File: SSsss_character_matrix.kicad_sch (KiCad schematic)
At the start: 17 parts, among them U15 SN74LVC244A, U16 10016AS, U17 10016AS, U18 SN74LVC244A, U19 10016AS, U20 10016AS, U21 10016AS

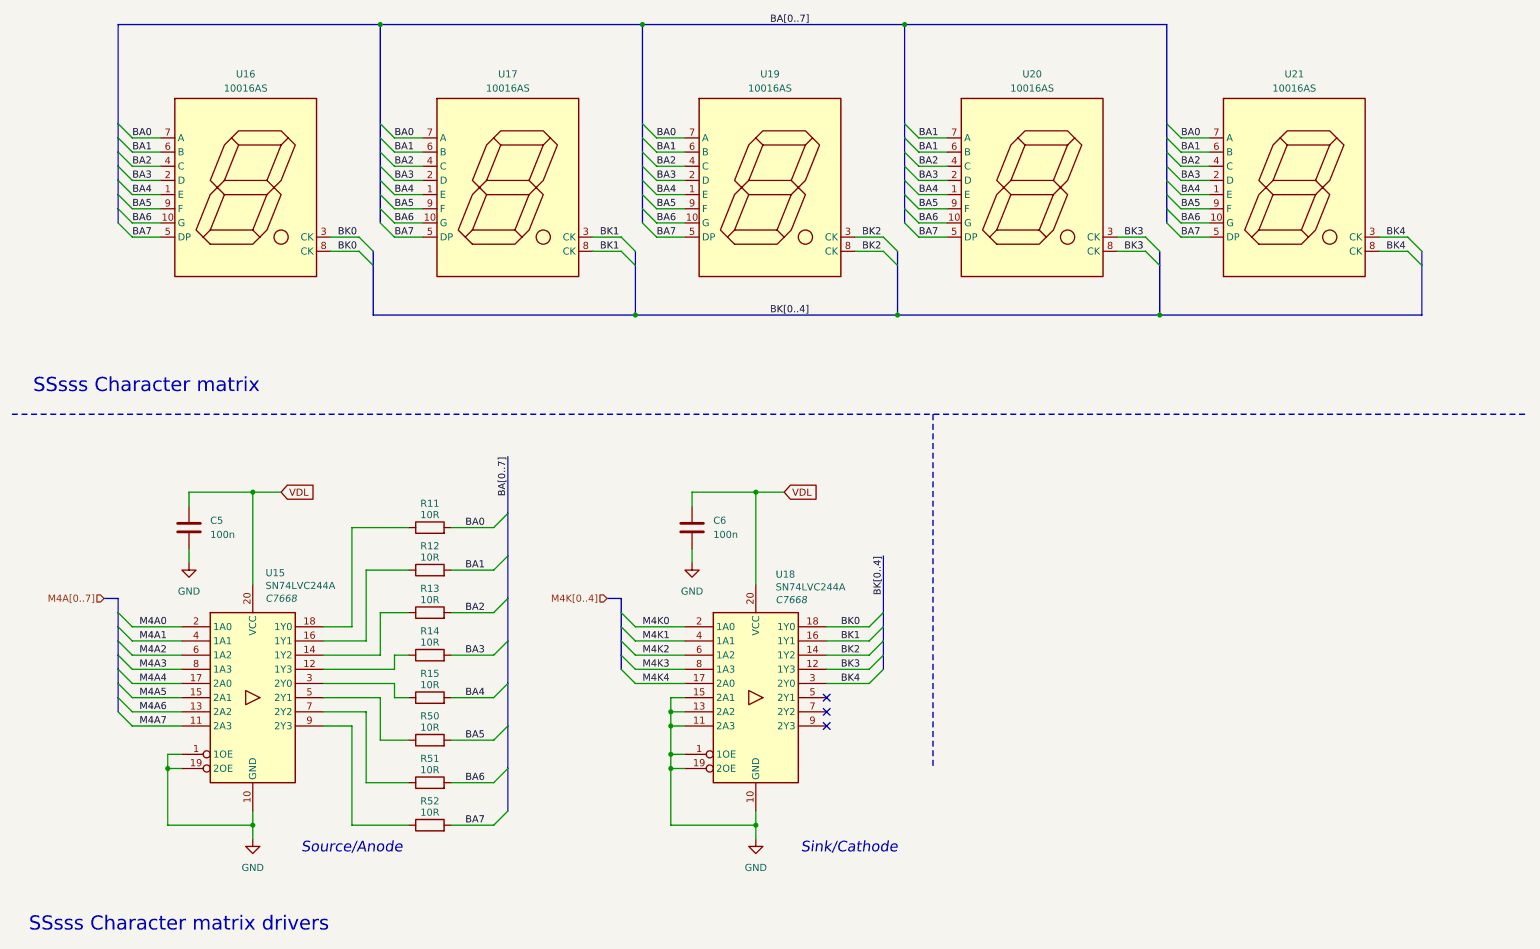
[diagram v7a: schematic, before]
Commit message: PCB routing
- JLCPCB constraints added
- removal of multiple test points
- change of footprints
- change of THT LEDs
- rough position of all the major components
- PCB routing started
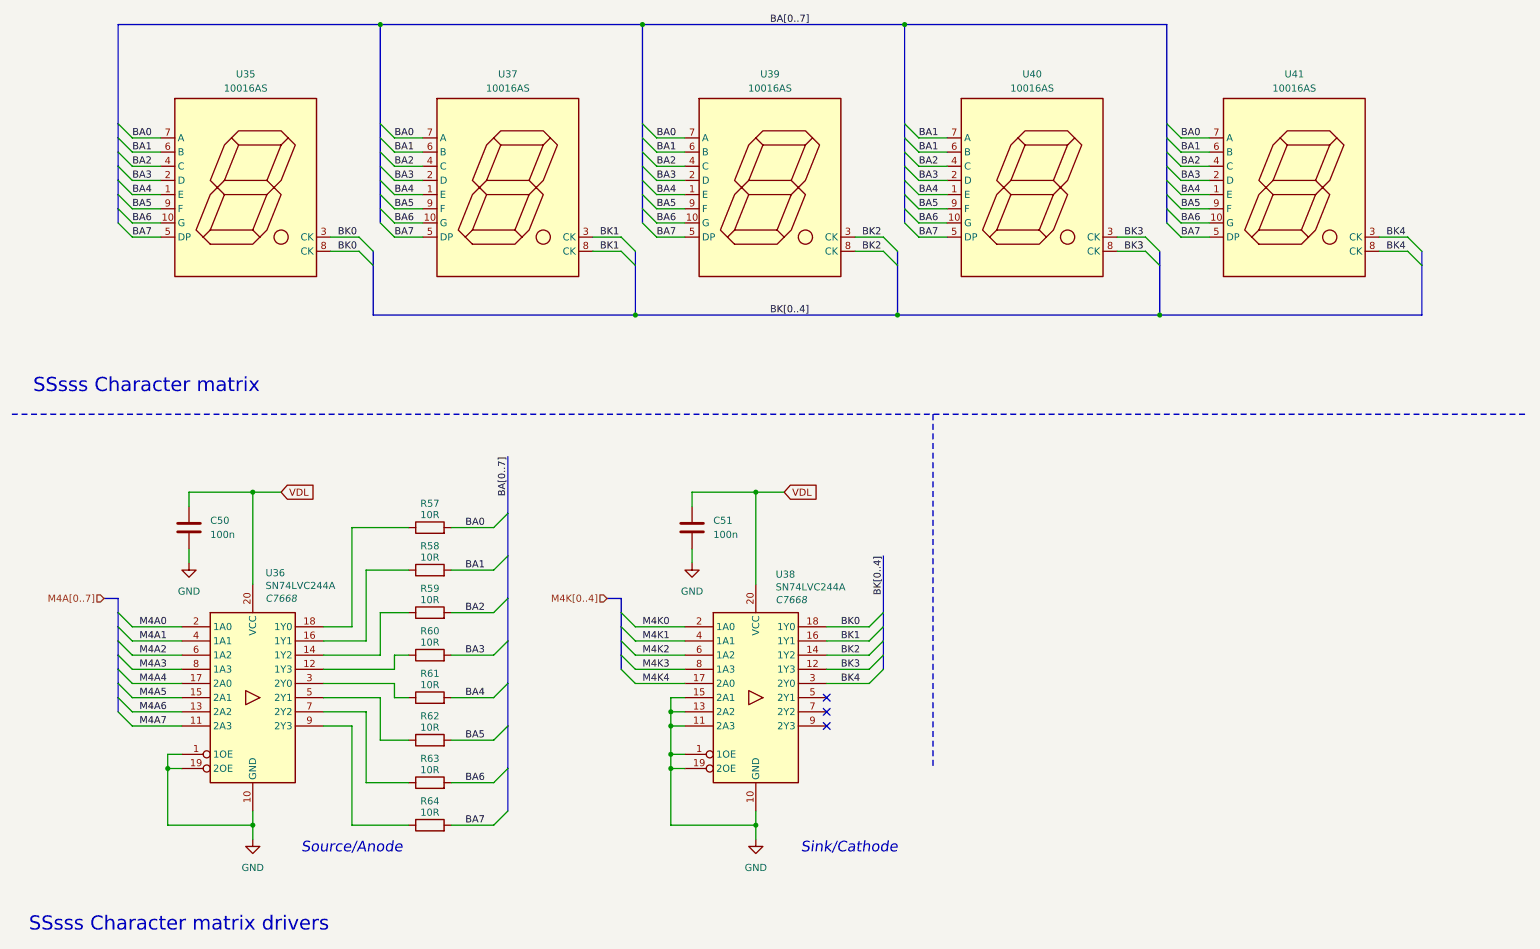
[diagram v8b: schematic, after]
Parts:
- U35: renamed from U16; footprint precision_clock:10016AS -> precision_clock:Xlitx 10016AS
- U37: renamed from U17; footprint precision_clock:10016AS -> precision_clock:Xlitx 10016AS
- U39: renamed from U19; footprint precision_clock:10016AS -> precision_clock:Xlitx 10016AS
- U40: renamed from U20; footprint precision_clock:10016AS -> precision_clock:Xlitx 10016AS
- U41: renamed from U21; footprint precision_clock:10016AS -> precision_clock:Xlitx 10016AS
- renumbered C5 to C50, C6 to C51, R11 to R57, R12 to R58, R13 to R59, R14 to R60, R15 to R61, R50 to R62, R51 to R63, R52 to R64, U15 to U36, U18 to U38
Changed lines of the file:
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@@
 		(on_board yes)
 		(dnp no)
-		(property "Reference" "R12"
+		(property "Reference" "R58"
 			(at 87.63 125.222 90)
 			(effects
@@
 			(project "Precision Clock"
 				(path "/c9a8ff63-a0d1-4125-9dd1-40fb53daf536/61b252ee-6ab4-4417-a4ad-7fc052d7ca20"
-					(reference "R12")
+					(reference "R58")
 					(unit 1)
 				)
@@
 		(dnp no)
 		(fields_autoplaced yes)
-		(property "Reference" "#PWR012"
+		(property "Reference" "#PWR0115"
 			(at 146.05 184.15 0)
 			(effects
@@
 			(project "Precision Clock"
 				(path "/c9a8ff63-a0d1-4125-9dd1-40fb53daf536/61b252ee-6ab4-4417-a4ad-7fc052d7ca20"
-					(reference "#PWR012")
+					(reference "#PWR0115")
 					(unit 1)
 				)
@@
 		(on_board yes)
 		(dnp no)
-		(property "Reference" "R51"
+		(property "Reference" "R63"
 			(at 87.63 163.322 90)
 			(effects
@@
 			(project "Precision Clock"
 				(path "/c9a8ff63-a0d1-4125-9dd1-40fb53daf536/61b252ee-6ab4-4417-a4ad-7fc052d7ca20"
-					(reference "R51")
+					(reference "R63")
 					(unit 1)
 				)
@@
 		(dnp no)
 		(fields_autoplaced yes)
-		(property "Reference" "U19"
+		(property "Reference" "U39"
 			(at 148.59 40.64 0)
 			(effects
@@
 			)
 		)
-		(property "Footprint" "precision_clock:10016AS"
+		(property "Footprint" "precision_clock:Xlitx 10016AS"
 			(at 148.59 60.96 0)
 			(effects
@@
 			(project "Precision Clock"
 				(path "/c9a8ff63-a0d1-4125-9dd1-40fb53daf536/61b252ee-6ab4-4417-a4ad-7fc052d7ca20"
-					(reference "U19")
+					(reference "U39")
 					(unit 1)
 				)
@@
 		(dnp no)
 		(fields_autoplaced yes)
-		(property "Reference" "C6"
+		(property "Reference" "C51"
 			(at 138.43 120.6499 0)
 			(effects
@@
 			(project "Precision Clock"
 				(path "/c9a8ff63-a0d1-4125-9dd1-40fb53daf536/61b252ee-6ab4-4417-a4ad-7fc052d7ca20"
-					(reference "C6")
+					(reference "C51")
 					(unit 1)
 				)
@@
 		(dnp no)
 		(fields_autoplaced yes)
-		(property "Reference" "#PWR09"
+		(property "Reference" "#PWR0112"
 			(at 44.45 134.62 0)
 			(effects
@@
 			(project "Precision Clock"
 				(path "/c9a8ff63-a0d1-4125-9dd1-40fb53daf536/61b252ee-6ab4-4417-a4ad-7fc052d7ca20"
-					(reference "#PWR09")
+					(reference "#PWR0112")
 					(unit 1)
 				)
@@
 		(dnp no)
 		(fields_autoplaced yes)
-		(property "Reference" "U21"
+		(property "Reference" "U41"
 			(at 242.57 40.64 0)
 			(effects
@@
 			)
 		)
-		(property "Footprint" "precision_clock:10016AS"
+		(property "Footprint" "precision_clock:Xlitx 10016AS"
 			(at 242.57 60.96 0)
 			(effects
@@
 			(project "Precision Clock"
 				(path "/c9a8ff63-a0d1-4125-9dd1-40fb53daf536/61b252ee-6ab4-4417-a4ad-7fc052d7ca20"
-					(reference "U21")
+					(reference "U41")
 					(unit 1)
 				)
@@
 		(on_board yes)
 		(dnp no)
-		(property "Reference" "R52"
+		(property "Reference" "R64"
 			(at 87.63 170.942 90)
 			(effects
@@
 			(project "Precision Clock"
 				(path "/c9a8ff63-a0d1-4125-9dd1-40fb53daf536/61b252ee-6ab4-4417-a4ad-7fc052d7ca20"
-					(reference "R52")
+					(reference "R64")
 					(unit 1)
 				)
@@
 		(on_board yes)
 		(dnp no)
-		(property "Reference" "U15"
+		(property "Reference" "U36"
 			(at 58.166 130.048 0)
 			(effects
@@
 			(project "Precision Clock"
 				(path "/c9a8ff63-a0d1-4125-9dd1-40fb53daf536/61b252ee-6ab4-4417-a4ad-7fc052d7ca20"
-					(reference "U15")
+					(reference "U36")
 					(unit 1)
 				)
@@
 		(on_board yes)
 		(dnp no)
-		(property "Reference" "R50"
+		(property "Reference" "R62"
 			(at 87.63 155.702 90)
 			(effects
@@
 			(project "Precision Clock"
 				(path "/c9a8ff63-a0d1-4125-9dd1-40fb53daf536/61b252ee-6ab4-4417-a4ad-7fc052d7ca20"
-					(reference "R50")
+					(reference "R62")
 					(unit 1)
 				)
@@
 		(dnp no)
 		(fields_autoplaced yes)
-		(property "Reference" "#PWR010"
+		(property "Reference" "#PWR0113"
 			(at 55.88 184.15 0)
 			(effects
@@
 			(project "Precision Clock"
 				(path "/c9a8ff63-a0d1-4125-9dd1-40fb53daf536/61b252ee-6ab4-4417-a4ad-7fc052d7ca20"
-					(reference "#PWR010")
+					(reference "#PWR0113")
 					(unit 1)
 				)
@@
 		(dnp no)
 		(fields_autoplaced yes)
-		(property "Reference" "U16"
+		(property "Reference" "U35"
 			(at 54.61 40.64 0)
 			(effects
@@
 			)
 		)
-		(property "Footprint" "precision_clock:10016AS"
+		(property "Footprint" "precision_clock:Xlitx 10016AS"
 			(at 54.61 60.96 0)
 			(effects
@@
 			(project "Precision Clock"
 				(path "/c9a8ff63-a0d1-4125-9dd1-40fb53daf536/61b252ee-6ab4-4417-a4ad-7fc052d7ca20"
-					(reference "U16")
+					(reference "U35")
 					(unit 1)
 				)
@@
 		(dnp no)
 		(fields_autoplaced yes)
-		(property "Reference" "#PWR011"
+		(property "Reference" "#PWR0114"
 			(at 134.62 134.62 0)
 			(effects
@@
 			(project "Precision Clock"
 				(path "/c9a8ff63-a0d1-4125-9dd1-40fb53daf536/61b252ee-6ab4-4417-a4ad-7fc052d7ca20"
-					(reference "#PWR011")
+					(reference "#PWR0114")
 					(unit 1)
 				)
@@
 		(dnp no)
 		(fields_autoplaced yes)
-		(property "Reference" "U20"
+		(property "Reference" "U40"
 			(at 195.58 40.64 0)
 			(effects
@@
 			)
 		)
-		(property "Footprint" "precision_clock:10016AS"
+		(property "Footprint" "precision_clock:Xlitx 10016AS"
 			(at 195.58 60.96 0)
 			(effects
@@
 			(project "Precision Clock"
 				(path "/c9a8ff63-a0d1-4125-9dd1-40fb53daf536/61b252ee-6ab4-4417-a4ad-7fc052d7ca20"
-					(reference "U20")
+					(reference "U40")
 					(unit 1)
 				)
@@
 		(dnp no)
 		(fields_autoplaced yes)
-		(property "Reference" "C5"
+		(property "Reference" "C50"
 			(at 48.26 120.6499 0)
 			(effects
@@
 			(project "Precision Clock"
 				(path "/c9a8ff63-a0d1-4125-9dd1-40fb53daf536/61b252ee-6ab4-4417-a4ad-7fc052d7ca20"
-					(reference "C5")
+					(reference "C50")
 					(unit 1)
 				)
@@
 		(on_board yes)
 		(dnp no)
-		(property "Reference" "R15"
+		(property "Reference" "R61"
 			(at 87.63 148.082 90)
 			(effects
@@
 			(project "Precision Clock"
 				(path "/c9a8ff63-a0d1-4125-9dd1-40fb53daf536/61b252ee-6ab4-4417-a4ad-7fc052d7ca20"
-					(reference "R15")
+					(reference "R61")
 					(unit 1)
 				)
@@
 		(on_board yes)
 		(dnp no)
-		(property "Reference" "R11"
+		(property "Reference" "R57"
 			(at 87.63 117.602 90)
 			(effects
@@
 			(project "Precision Clock"
 				(path "/c9a8ff63-a0d1-4125-9dd1-40fb53daf536/61b252ee-6ab4-4417-a4ad-7fc052d7ca20"
-					(reference "R11")
+					(reference "R57")
 					(unit 1)
 				)
@@
 		(on_board yes)
 		(dnp no)
-		(property "Reference" "R14"
+		(property "Reference" "R60"
 			(at 87.63 140.462 90)
 			(effects
@@
 			(project "Precision Clock"
 				(path "/c9a8ff63-a0d1-4125-9dd1-40fb53daf536/61b252ee-6ab4-4417-a4ad-7fc052d7ca20"
-					(reference "R14")
+					(reference "R60")
 					(unit 1)
 				)
@@
 		(on_board yes)
 		(dnp no)
-		(property "Reference" "R13"
+		(property "Reference" "R59"
 			(at 87.63 132.842 90)
 			(effects
@@
 			(project "Precision Clock"
 				(path "/c9a8ff63-a0d1-4125-9dd1-40fb53daf536/61b252ee-6ab4-4417-a4ad-7fc052d7ca20"
-					(reference "R13")
+					(reference "R59")
 					(unit 1)
 				)
@@
 		(on_board yes)
 		(dnp no)
-		(property "Reference" "U18"
+		(property "Reference" "U38"
 			(at 149.606 130.302 0)
 			(effects
@@
 			(project "Precision Clock"
 				(path "/c9a8ff63-a0d1-4125-9dd1-40fb53daf536/61b252ee-6ab4-4417-a4ad-7fc052d7ca20"
-					(reference "U18")
+					(reference "U38")
 					(unit 1)
 				)
@@
 		(dnp no)
 		(fields_autoplaced yes)
-		(property "Reference" "U17"
+		(property "Reference" "U37"
 			(at 101.6 40.64 0)
 			(effects
@@
 			)
 		)
-		(property "Footprint" "precision_clock:10016AS"
+		(property "Footprint" "precision_clock:Xlitx 10016AS"
 			(at 101.6 60.96 0)
 			(effects
@@
 			(project "Precision Clock"
 				(path "/c9a8ff63-a0d1-4125-9dd1-40fb53daf536/61b252ee-6ab4-4417-a4ad-7fc052d7ca20"
-					(reference "U17")
-					(unit 1)
-				)
+					(reference "U37")
+					(unit 1)
+				)
